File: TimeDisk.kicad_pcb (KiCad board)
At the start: 4 copper layers, 107.6 x 59.8 mm, 80 parts, among them J1 AppleIIBus, J2 microUSB, J3 JTAG, Q1 AO3401A, SW1 Mode, U1 EPM7128SL84, U2 DS1315S-5, U3 74LVC04AD, U4 AS6C8008, U5 39F040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

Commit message: Update via-to-via clearance rules and update footprints
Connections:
- U3 pad 7: unconnected-(U3G-GND-Pad7) -> GND
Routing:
- net Net-(BT1-+): track 125.2 -> 120.0 mm
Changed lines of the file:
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@@
   (net 126 "Net-(D1-A)")
   (net 127 "Net-(D3-A)")
-  (net 128 "unconnected-(U3G-GND-Pad7)")
   (footprint "stdpads:C_0805" (layer "F.Cu")
     (at 171.108 85.725 180)
@@
     (property "ki_description" "Generic connector, double row, 02x25, counter clockwise pin numbering scheme (similar to DIP packge numbering), script generated (kicad-library-utils/schlib/autogen/connector/)")
     (property "ki_keywords" "connector")
-    (attr exclude_from_pos_files)
+    (attr exclude_from_pos_files allow_soldermask_bridges)
     (fp_text reference "J1" (at 0 4.953) (layer "F.Fab")
         (effects (font (size 0.8128 0.8128) (thickness 0.2032)))
@@
     (property "ki_keywords" "battery cell")
     (attr smd)
-    (fp_text reference "BT1" (at 0 0 -135) (layer "F.Fab")
-        (effects (font (size 0.8128 0.8128) (thickness 0.2032)))
-    )
-    (fp_text value "CR2032" (at 0 -5.08 -135) (layer "F.Fab")
+    (fp_text reference "BT1" (at 0 0 45) (layer "F.Fab")
         (effects (font (size 0.8128 0.8128) (thickness 0.2032)))
     )
-    (fp_text user "${REFERENCE}" (at 0 -6.35 -135) (layer "F.SilkS")
+    (fp_text value "CR2032" (at 0 -5.08 45) (layer "F.Fab")
         (effects (font (size 0.8128 0.8128) (thickness 0.2032)))
     )
@@
         (effects (font (size 0.254 0.254) (thickness 0.0635)))
     )
-    (fp_text value "10u" (at 0 0.35) (layer "F.Fab")
+    (fp_text value "10u" (at 0 0.35 180) (layer "F.Fab")
         (effects (font (size 0.254 0.254) (thickness 0.0635)))
     )
@@
       (net 107 "Net-(R9-Pad1)") (pintype "output"))
     (pad "7" smd roundrect (at 3.81 2.475) (size 1.95 0.6) (layers "F.Cu" "F.Paste" "F.Mask") (roundrect_rratio 0.25)
-      (net 128 "unconnected-(U3G-GND-Pad7)") (pinfunction "GND") (pintype "power_in"))
+      (net 2 "GND") (pinfunction "GND") (pintype "power_in"))
     (pad "8" smd roundrect (at 3.81 -2.475) (size 1.95 0.6) (layers "F.Cu" "F.Paste" "F.Mask") (roundrect_rratio 0.25)
       (net 78 "unconnected-(U3-Pad8)") (pintype "output+no_connect"))
@@
     (property "ki_keywords" "quartz ceramic resonator oscillator")
     (attr through_hole)
-    (fp_text reference "Y1" (at 1.016 5.715 90) (layer "F.SilkS")
-        (effects (font (size 0.8128 0.8128) (thickness 0.2032) bold))
+    (fp_text reference "Y1" (at -1.6 1.75 90) (layer "F.SilkS") hide
+        (effects (font (size 1 1) (thickness 0.15)))
     )
-    (fp_text value "32k768" (at 1.016 5.9055 90) (layer "F.Fab")
-        (effects (font (size 0.8128 0.8128) (thickness 0.2032) bold))
+    (fp_text value "32k768" (at 3.5 1.75 90) (layer "F.Fab")
+        (effects (font (size 1 1) (thickness 0.15)))
     )
-    (fp_text user "${REFERENCE}" (at 1 2.794 180) (layer "F.Fab")
-        (effects (font (size 0.8128 0.8128) (thickness 0.2032) bold))
+    (fp_text user "${REFERENCE}" (at 1 5.5 90) (layer "F.Fab")
+        (effects (font (size 0.7 0.7) (thickness 0.105)))
     )
     (fp_line (start -0.28 1.8) (end -0.28 8.7)
@@
         (effects (font (size 0.254 0.254) (thickness 0.0635)))
     )
-    (fp_text user "${REFERENCE}" (at 0 0 90) (layer "F.SilkS") hide
+    (fp_text user "${REFERENCE}" (at 0 0 270) (layer "F.SilkS") hide
         (effects (font (size 0.254 0.254) (thickness 0.0635)))
     )
@@
     (solder_paste_margin -0.025)
     (attr smd)
-    (fp_text reference "D2" (at 0 0) (layer "F.Fab")
+    (fp_text reference "D2" (at 0 0 180) (layer "F.Fab")
         (effects (font (size 0.508 0.508) (thickness 0.127)))
     )
-    (fp_text value "1N5819" (at 0 0.75) (layer "F.Fab")
+    (fp_text value "1N5819" (at 0 0.75 180) (layer "F.Fab")
         (effects (font (size 0.127 0.127) (thickness 0.03175)))
     )
@@
     (property "Sheetfile" "TimeDisk.kicad_sch")
     (property "Sheetname" "")
-    (solder_mask_margin 0.025)
-    (solder_paste_margin -0.05)
+    (solder_mask_margin 0.035)
+    (solder_paste_margin -0.025)
     (attr smd)
     (fp_text reference "U8" (at 0 0 180) (layer "F.Fab")
@@
     (solder_paste_margin -0.025)
     (attr smd)
-    (fp_text reference "R14" (at 0 0) (layer "F.Fab")
+    (fp_text reference "R14" (at 0 0 180) (layer "F.Fab")
         (effects (font (size 0.254 0.254) (thickness 0.0635)))
     )
-    (fp_text value "220" (at 0 0.35) (layer "F.Fab")
+    (fp_text value "220" (at 0 0.35 180) (layer "F.Fab")
         (effects (font (size 0.254 0.254) (thickness 0.0635)))
     )
@@
     (solder_paste_margin -0.025)
     (attr smd)
-    (fp_text reference "D3" (at 0 0) (layer "F.Fab")
+    (fp_text reference "D3" (at 0 0 180) (layer "F.Fab")
         (effects (font (size 0.254 0.254) (thickness 0.0635)))
     )
-    (fp_text value "10V" (at 0 0.55) (layer "F.Fab")
+    (fp_text value "10V" (at 0 0.55 180) (layer "F.Fab")
         (effects (font (size 0.127 0.127) (thickness 0.03175)))
     )
-    (fp_line (start -1.8 -0.85) (end -1.8 0.85)
+    (fp_line (start -1.85 -0.85) (end -1.85 0.85)
       (stroke (width 0.12) (type solid)) (layer "F.SilkS"))
-    (fp_line (start -1.8 -0.85) (end 1.05 -0.85)
+    (fp_line (start -1.85 -0.85) (end 1.05 -0.85)
       (stroke (width 0.12) (type solid)) (layer "F.SilkS"))
-    (fp_line (start -1.8 0.85) (end 1.05 0.85)
+    (fp_line (start -1.85 0.85) (end 1.05 0.85)
       (stroke (width 0.12) (type solid)) (layer "F.SilkS"))
     (fp_line (start -1.95 -1) (end -1.95 1)
@@
         (effects (font (size 0.508 0.508) (thickness 0.127)))
     )
-    (fp_line (start -2.15 -0.85) (end -2.15 1.75)
+    (fp_line (start -2.15 1.1) (end -2.15 1.8)
       (stroke (width 0.1524) (type solid)) (layer "F.SilkS"))
-    (fp_line (start -2.15 1.75) (end 1.1 1.75)
+    (fp_line (start -2.15 1.8) (end -1.45 1.8)
       (stroke (width 0.1524) (type solid)) (layer "F.SilkS"))
     (fp_line (start -2.1 -1.7) (end -2.1 1.7)
@@
     (solder_paste_margin -0.05)
     (attr smd)
-    (fp_text reference "Q1" (at 0 0) (layer "F.Fab")
+    (fp_text reference "Q1" (at 0 0 180) (layer "F.Fab")
         (effects (font (size 0.381 0.381) (thickness 0.09525)))
     )
-    (fp_text value "AO3401A" (at 0.45 0) (layer "F.Fab")
+    (fp_text value "AO3401A" (at 0.45 0 180) (layer "F.Fab")
         (effects (font (size 0.127 0.127) (thickness 0.03175)))
     )
@@
     (pad "2" smd roundrect (at 0.95 0) (size 0.85 1.4) (layers "F.Cu" "F.Paste" "F.Mask") (roundrect_rratio 0.25)
       (net 1 "+5V") (pintype "passive"))
+    (model "${KICAD6_3DMODEL_DIR}/Resistor_SMD.3dshapes/R_0805_2012Metric.wrl"
+      (offset (xyz 0 0 0))
+      (scale (xyz 1 1 1))
+      (rotate (xyz 0 0 0))
+    )
   )
   (footprint "LOGO" (layer "B.Cu")
@@
         (effects (font (size 0.508 0.508) (thickness 0.127)) (justify mirror))
     )
-    (fp_text value "JTAG" (at 0 -4.191 90) (layer "B.SilkS") hide
+    (fp_text value "JTAG" (at 0 -4.191 90) (layer "B.SilkS")
         (effects (font (size 0.8128 0.8128) (thickness 0.2032)) (justify mirror))
     )
@@
         (effects (font (size 0.8128 0.8128) (thickness 0.2032)) (justify mirror))
     )
+    (fp_line (start -3.3 2.7) (end -3.3 -3.302)
+      (stroke (width 0.127) (type solid)) (layer "B.SilkS"))
+    (fp_line (start 3.3 2.7) (end 3.3 -2.7)
+      (stroke (width 0.127) (type solid)) (layer "B.SilkS"))
     (fp_line (start -3.937 -3.556) (end 3.937 -3.556)
       (stroke (width 0.05) (type solid)) (layer "B.CrtYd"))
@@
   (via (at 145.415 101.346) (size 0.8) (drill 0.4) (layers "F.Cu" "B.Cu") (net 125))
   (segment (start 147.85975 103.85425) (end 164.465 87.249) (width 1.524) (layer "B.Cu") (net 125))
-  (segment (start 155.2575 101.4095) (end 165.989 90.678) (width 1.524) (layer "B.Cu") (net 125))
   (segment (start 148.463 106.299) (end 146.939 104.775) (width 1.524) (layer "B.Cu") (net 125))
+  (segment (start 165.989 90.678) (end 155.2575 101.4095) (width 1.524) (layer "B.Cu") (net 125))
   (segment (start 145.415 101.346) (end 145.415 103.251) (width 1.524) (layer "B.Cu") (net 125))
   (segment (start 150.368 106.299) (end 148.463 106.299) (width 1.524) (layer "B.Cu") (net 125))
@@
   (segment (start 145.415 101.346) (end 150.368 106.299) (width 1.524) (layer "B.Cu") (net 125))
   (segment (start 164.465 87.249) (end 165.989 88.773) (width 1.524) (layer "B.Cu") (net 125))
-  (segment (start 145.542 103.378) (end 145.415 103.251) (width 0.8) (layer "B.Cu") (net 125))
-  (segment (start 150.368 106.299) (end 155.2575 101.4095) (width 1.524) (layer "B.Cu") (net 125))
   (segment (start 165.989 88.773) (end 165.989 90.678) (width 1.524) (layer "B.Cu") (net 125))
   (segment (start 146.558 104.775) (end 146.939 104.775) (width 0.8) (layer "B.Cu") (net 125))
   (segment (start 145.415 103.251) (end 146.939 104.775) (width 1.524) (layer "B.Cu") (net 125))
+  (segment (start 155.2575 101.4095) (end 150.368 106.299) (width 1.524) (layer "B.Cu") (net 125))
   (segment (start 147.85975 104.552749) (end 147.85975 103.85425) (width 0.8) (layer "B.Cu") (net 125))
   (segment (start 165.989 90.678) (end 161.036 85.725) (width 1.524) (layer "B.Cu") (net 125))
-  (segment (start 155.2575 101.4095) (end 151.765 104.902) (width 1.524) (layer "B.Cu") (net 125))
   (segment (start 148.8 107.05) (end 148.8 108.2) (width 0.6) (layer "F.Cu") (net 126))
   (segment (start 148.05 106.3) (end 148.8 107.05) (width 0.6) (layer "F.Cu") (net 126))

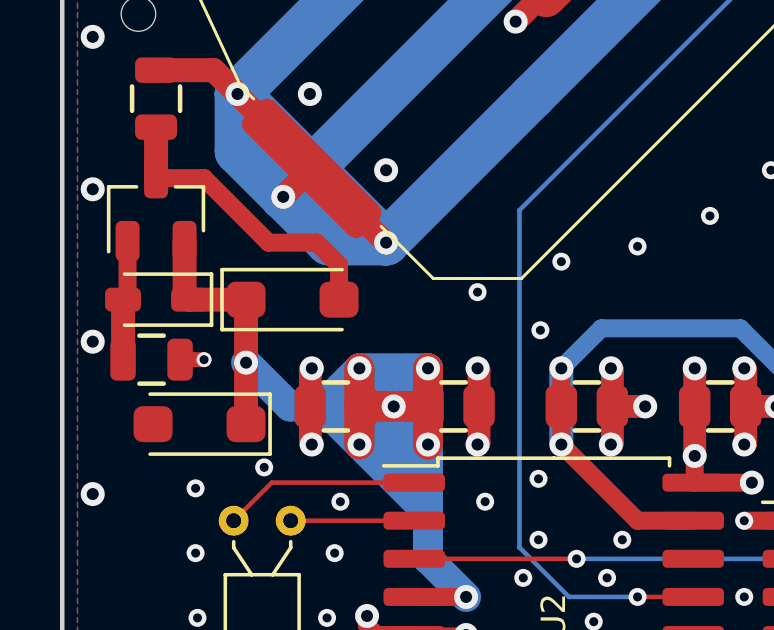
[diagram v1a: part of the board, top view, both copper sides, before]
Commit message: with hole
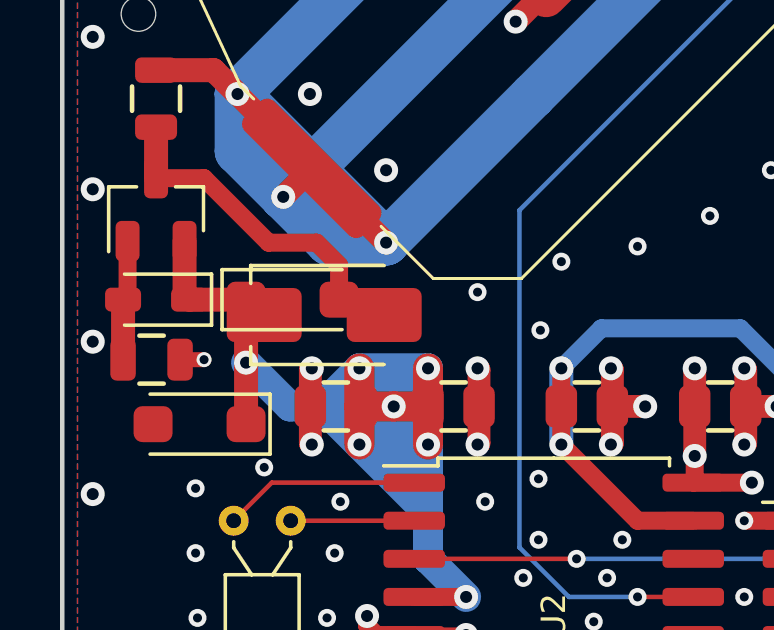
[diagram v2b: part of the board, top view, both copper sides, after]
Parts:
- added REF**: D_SMA, stdpads:D_SMA, F.Cu at (148.3, 108.7)
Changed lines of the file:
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@@
   )
   (paper "A4")
+  (title_block
+    (title "GW4206B (TimeDisk)")
+    (date "2024-03-21")
+    (rev "1.1")
+    (company "Garrett's Workshop")
+  )
   (layers
     (0 "F.Cu" signal)
@@
       (offset (xyz 0 0 0))
       (scale (xyz 1 1 1))
+      (rotate (xyz 0 0 0))
+    )
+  )
+  (footprint "stdpads:D_SMA" (layer "F.Cu")
+    (at 148.3045 108.712)
+    (descr "Diode SMA (DO-214AC)")
+    (tags "Diode SMA (DO-214AC)")
+    (solder_mask_margin 0.05)
+    (solder_paste_margin -0.025)
+    (attr smd)
+    (fp_text reference "REF**" (at 0 -1.1 180) (layer "F.Fab")
+        (effects (font (size 0.381 0.381) (thickness 0.09525)))
+    )
+    (fp_text value "D_SMA" (at 0 1.1) (layer "F.Fab")
+        (effects (font (size 0.381 0.381) (thickness 0.09525)))
+    )
+    (fp_line (start -2.45 -1.65) (end -2.45 -1.05)
+      (stroke (width 0.12) (type solid)) (layer "F.SilkS"))
+    (fp_line (start -2.45 -1.65) (end 2 -1.65)
+      (stroke (width 0.12) (type solid)) (layer "F.SilkS"))
+    (fp_line (start -2.45 1.05) (end -2.45 1.65)
+      (stroke (width 0.12) (type solid)) (layer "F.SilkS"))
+    (fp_line (start -2.45 1.65) (end 2 1.65)
+      (stroke (width 0.12) (type solid)) (layer "F.SilkS"))
+    (fp_line (start -3.5 -1.75) (end 3.5 -1.75)
+      (stroke (width 0.05) (type solid)) (layer "F.CrtYd"))
+    (fp_line (start -3.5 1.75) (end -3.5 -1.75)
+      (stroke (width 0.05) (type solid)) (layer "F.CrtYd"))
+    (fp_line (start 3.5 -1.75) (end 3.5 1.75)
+      (stroke (width 0.05) (type solid)) (layer "F.CrtYd"))
+    (fp_line (start 3.5 1.75) (end -3.5 1.75)
+      (stroke (width 0.05) (type solid)) (layer "F.CrtYd"))
+    (fp_line (start -2.3 1.5) (end -2.3 -1.5)
+      (stroke (width 0.1) (type solid)) (layer "F.Fab"))
+    (fp_line (start -0.64944 -0.79908) (end -0.64944 0.80112)
+      (stroke (width 0.1) (type solid)) (layer "F.Fab"))
+    (fp_line (start -0.64944 0.00102) (end -1.55114 0.00102)
+      (stroke (width 0.1) (type solid)) (layer "F.Fab"))
+    (fp_line (start -0.64944 0.00102) (end 0.50118 -0.79908)
+      (stroke (width 0.1) (type solid)) (layer "F.Fab"))
+    (fp_line (start -0.64944 0.00102) (end 0.50118 0.75032)
+      (stroke (width 0.1) (type solid)) (layer "F.Fab"))
+    (fp_line (start 0.50118 0.00102) (end 1.4994 0.00102)
+      (stroke (width 0.1) (type solid)) (layer "F.Fab"))
+    (fp_line (start 0.50118 0.75032) (end 0.50118 -0.79908)
+      (stroke (width 0.1) (type solid)) (layer "F.Fab"))
+    (fp_line (start 2.3 -1.5) (end -2.3 -1.5)
+      (stroke (width 0.1) (type solid)) (layer "F.Fab"))
+    (fp_line (start 2.3 -1.5) (end 2.3 1.5)
+      (stroke (width 0.1) (type solid)) (layer "F.Fab"))
+    (fp_line (start 2.3 1.5) (end -2.3 1.5)
+      (stroke (width 0.1) (type solid)) (layer "F.Fab"))
+    (pad "1" smd roundrect (at -2 0) (size 2.5 1.8) (layers "F.Cu" "F.Paste" "F.Mask") (roundrect_rratio 0.15))
+    (pad "2" smd roundrect (at 2 0) (size 2.5 1.8) (layers "F.Cu" "F.Paste" "F.Mask") (roundrect_rratio 0.15))
+    (model "${KICAD6_3DMODEL_DIR}/Diode_SMD.3dshapes/D_SMA.wrl"
+      (offset (xyz 0 0 0))
+      (scale (xyz 1 1 1))

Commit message: RC 1.1
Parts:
- removed R1: DNP, stdpads:R_0805
- removed R15: 4k7, stdpads:R_0805
- removed R3: 1k, stdpads:R_0805
- removed REF**: D_SMA, stdpads:D_SMA
- D3: value 10V -> 6V8
- R11, R13: value 22k -> DNP
- U8: footprint stdpads:NXP_VSSOP-8_2.3x2mm -> stdpads:NXP_TSSOP-8_3x3mm_P0.65mm
- moved C29 7.14 mm to (191.7, 83.8), turned to 0 degrees
- moved U8 4.87 mm to (191.8, 87.7), turned to 90 degrees
- moved R16 3.17 mm to (195.4, 83.8)
- moved J2 0.55 mm to (234.8, 81.8)
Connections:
- U7 pad 12: /~{DCD} -> +5V
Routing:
- net +3V3: track 54.0 -> 82.7 mm, vias 2 -> 6
- net /~{DCD}: track 18.4 -> 0.00 mm, vias 2 -> 0
- net /RA2: track 24.1 -> 13.9 mm
- net /IRQ~{OE}: track 93.6 -> 89.8 mm
- net Net-(U8-Q): track 6.82 -> 3.26 mm
- net /RA0: track 20.4 -> 23.2 mm
- net /RA1: track 23.5 -> 25.2 mm
- net /RAMCS: track 41.4 -> 42.9 mm
- net GND: track 189.2 -> 187.8 mm, vias 483 -> 488
- net +5V: track 119.1 -> 119.7 mm
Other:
- board text added: "!"
- board text added: "Positive Up"
- board text added: "Toward Rear"
